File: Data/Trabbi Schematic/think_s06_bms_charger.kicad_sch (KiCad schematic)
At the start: 13 parts, among them J1 230V AC Mains Connection, K1 230V Relay, K2 Charge Cooling Relay R4, M1 Radiator Fan A (E11A), M2 Radiator Fan B (E11B), M3 Coolant Pump (E16), SW1 Charge Current Switch, U1 Battery Monitoring System (E0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, U2 Charger (E03)

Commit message: Fix wire-to-pin connections: use exact calculated pin positions
Refactored gen_think_complete.py to compute exact pin schematic
coordinates instead of using approximate manual offsets. Added p()
method to Sheet class that transforms symbol-local pin positions to
schematic coordinates. All 232 wire calls across 13 sub-sheet
generators now use p() for pin endpoints, fixing misaligned
connections (previously off by 0.54-10+ units).

Co-Authored-By: Claude Opus 4.6 <noreply@anthropic.com>
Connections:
- net +114V_CHARGER: now also U2.4 (+114V_DC)
- net +12V_F10_WPUMP_CHG: now also M3.1 (M+)
- net +12V_F28_DRIVE: now also U1.1 (BAT_12V)
- net +12V_F6_RADFAN: now also M1.1 (M+), M2.1 (M+)
- net -114V_CHARGER: now also U2.5 (-114V_DC)
- net BATT_COOLING: now also K2.1 (86_COIL+), U1.13 (BATT_COOLING)
- net BMS_CMD: now also U1.7 (BMS_CMD)
- net CHG_START: now also U2.6 (CHG_START)
- net CHG_START_IN: now also U1.4 (CHG_START_IN)
- net CHG_START_OUT: now also U1.6 (CHG_START_OUT)
- net CHG_STATUS_OK: now also U1.5 (CHG_STATUS_OK), U2.7 (CHG_STATUS_OK)
- net CURR_SENSE: now also U1.12 (CURR_SENSE)
- net CURR_S_12V: now also U1.10 (CURR_S_12V)
- net CURR_S_GND: now also U1.11 (CURR_S_GND)
- net DC_LO_PWR: now also U1.3 (DC_LO_PWR)
- net GND: now also M1.2 (M-), M2.2 (M-), M3.2 (M-), U1.2 (BAT_GND)
- net GND_AC: now also U2.3 (GND_AC)
- net K_LINE: now also U1.8 (K_LINE), U2.8 (K_LINE)
- net L1_AC: now also U2.1 (L1_AC)
- net L2_AC: now also U2.2 (L2_AC)
- net L_LINE: now also U1.9 (L_LINE), U2.9 (L_LINE)
- net TEMP1: now also RT1.1 (T+), U1.14 (TEMP1)
- net TEMP2: now also RT2.1 (T+), U1.15 (TEMP2)
- net TEMP3: now also RT3.1 (T+), U1.16 (TEMP3)
- net TEMP4: now also RT4.1 (T+), U1.17 (TEMP4)
- net at J1.1 (L1): now also K1.3 (30_COM)

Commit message: Enforce orthogonal routing and 1.27mm grid alignment
- Add _g() grid snap function to Sheet class (rounds all coordinates to nearest 1.27mm)
- Add wire_l() method for L-shaped orthogonal routing (horizontal+vertical segments)
- Apply grid snapping in p(), place(), wire(), label(), glabel(), junction(), no_connect(), defsym()
- Replace all 19 diagonal wire calls with wire_l() across S02, S06, S07, S08, S10, S12, S13
- All wire segments now strictly horizontal or vertical, no diagonals
- All coordinates verified on 1.27mm (50mil) KiCad standard grid

Co-Authored-By: Claude Opus 4.6 <noreply@anthropic.com>
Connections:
- net TEMP2 is gone; now on net TEMP1: RT2.1 (T+), U1.15 (TEMP2)
- net TEMP3 is gone; now on net TEMP1: RT3.1 (T+), U1.16 (TEMP3)
- net TEMP4 is gone; now on net TEMP1: RT4.1 (T+), U1.17 (TEMP4)
- net 230V_L1: now also J1.1 (L1), K1.3 (30_COM)

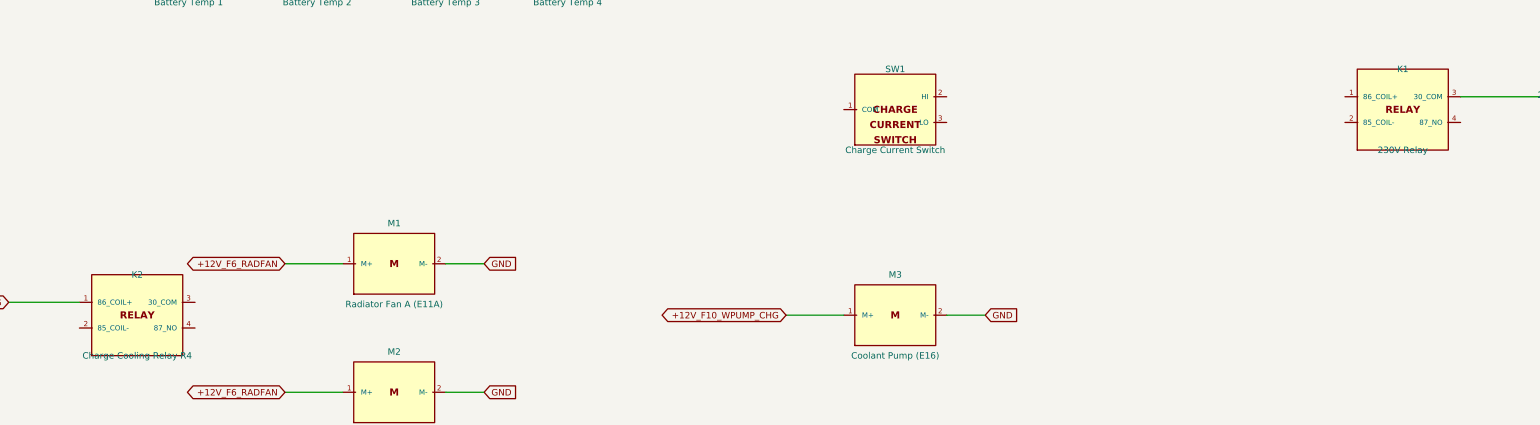
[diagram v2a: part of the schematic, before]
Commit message: Add relay coil/switch graphics, fix label positioning
- Draw coil (inductor arcs) and switch contacts (circles + arm)
  inside RELAY_SPST and RELAY_SPDT symbol bodies
- Add body_gfx parameter to defsym() for custom symbol graphics
- Helper functions: _gfx_polyline, _gfx_arc, _gfx_circle, _relay_gfx
- Fix label offsets: increase from 3-5mm to 10-12mm to avoid
  overlapping pin names (S01 ignition, S02 HV, S05 DCDC, S07 lights)
- Fix S09 turn signal rear labels: add wire stubs (were at 0 offset)
- All 14 schematics regenerated, parentheses balanced, grid OK

Co-Authored-By: Claude Opus 4.6 <noreply@anthropic.com>
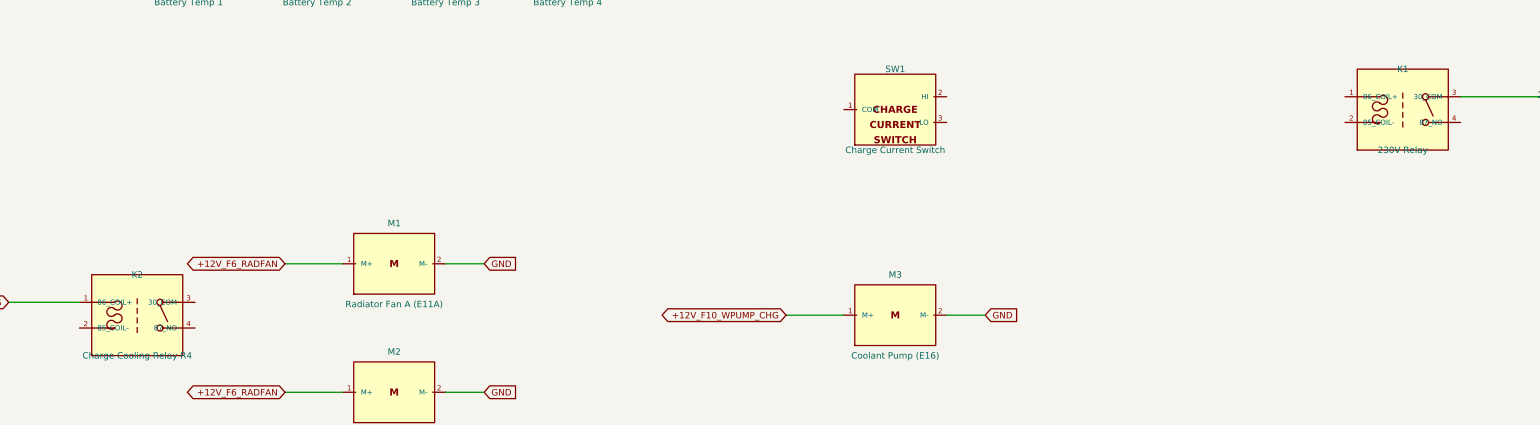
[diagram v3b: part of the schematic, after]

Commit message: Fix label/text positioning: Ref/Value outside body, hide pin numbers
- Reference placed above body edge, Value below (dynamic based on
  symbol height) — no longer overlapping body text
- Pin numbers hidden (clutter, not useful in schematic view)
- Pin name font reduced from 1.016mm to 0.762mm (less overlap)
- Pin length increased from 2.54mm to 3.81mm (more room for pin names
  between body edge and endpoint)
- Store symbol dimensions in _sym_dims for dynamic property placement

Co-Authored-By: Claude Opus 4.6 <noreply@anthropic.com>
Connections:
- net TEMP1: now also RT2.2 (T-)

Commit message: Add cross-sheet reference annotations to global labels
- Track all global label positions per sheet during build
- After building all sheets, annotate each global label with
  "→S01,S03,..." text showing which other sheets share the net
- 60 cross-sheet nets identified and annotated
- Two-pass build: 1) build all sheets 2) add cross-refs + save
- Text placed near label in 0.8mm font, offset to avoid overlap

Co-Authored-By: Claude Opus 4.6 <noreply@anthropic.com>
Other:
- note added: "→S01"
- note added: "→S01,S02,S03,S04,S05,S07,S08,S09,S10,S11,S12,S13"
- note added: "→S01,S02,S13"
- note added: "→S01,S11"
- note added: "→S02,S03,S11"
- note added: "→S02,S03,S11,S13"
- note added: "→S02,S03,S13"
- note added: "→S02,S13"
- note added: "→S03"
- note added: "→S05"
- note added: "→S11"
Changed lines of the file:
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@@
     (effects (font (size 1.000 1.000)))
+  )
+  (text "→S01,S02,S13" (at 56.690 86.320 0)
+    (effects (font (size 0.800 0.800)))
+  )
+  (text "→S01,S02,S03,S04,S05,S07,S08,S09,S10,S11,S12,S13" (at 56.690 97.750 0)
+    (effects (font (size 0.800 0.800)))
+  )
+  (text "→S01,S02,S03,S04,S05,S07,S08,S09,S10,S11,S12,S13" (at 122.380 232.370 0)
+    (effects (font (size 0.800 0.800)))
+  )
+  (text "→S01,S02,S03,S04,S05,S07,S08,S09,S10,S11,S12,S13" (at 122.380 257.770 0)
+    (effects (font (size 0.800 0.800)))
+  )
+  (text "→S01,S02,S03,S04,S05,S07,S08,S09,S10,S11,S12,S13" (at 221.440 242.530 0)
+    (effects (font (size 0.800 0.800)))
+  )
+  (text "→S05" (at 56.690 107.910 0)
+    (effects (font (size 0.800 0.800)))
+  )
+  (text "→S03" (at 143.970 85.050 0)
+    (effects (font (size 0.800 0.800)))
+  )
+  (text "→S03" (at 297.640 61.500 0)
+    (effects (font (size 0.800 0.800)))
+  )
+  (text "→S02,S03,S13" (at 143.970 102.830 0)
+    (effects (font (size 0.800 0.800)))
+  )
+  (text "→S02,S03,S11,S13" (at 143.970 111.720 0)
+    (effects (font (size 0.800 0.800)))
+  )
+  (text "→S02,S03,S11,S13" (at 307.800 139.160 0)
+    (effects (font (size 0.800 0.800)))
+  )
+  (text "→S02,S03,S11" (at 143.970 120.610 0)
+    (effects (font (size 0.800 0.800)))
+  )
+  (text "→S02,S03,S11" (at 297.640 139.160 0)
+    (effects (font (size 0.800 0.800)))
+  )
+  (text "→S11" (at 91.900 55.150 0)
+    (effects (font (size 0.800 0.800)))
+  )
+  (text "→S11" (at 19.860 239.990 0)
+    (effects (font (size 0.800 0.800)))
+  )
+  (text "→S05" (at 337.010 96.480 0)
+    (effects (font (size 0.800 0.800)))
+  )
+  (text "→S05" (at 337.010 109.180 0)
+    (effects (font (size 0.800 0.800)))
+  )
+  (text "→S02,S13" (at 307.800 61.500 0)
+    (effects (font (size 0.800 0.800)))
+  )
+  (text "→S01" (at 74.470 232.370 0)
+    (effects (font (size 0.800 0.800)))
+  )
+  (text "→S01" (at 74.470 257.770 0)
+    (effects (font (size 0.800 0.800)))
+  )
+  (text "→S01,S11" (at 173.530 242.530 0)
+    (effects (font (size 0.800 0.800)))
   )
   (symbol_instances)

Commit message: Fix label text justification for KiCad 9
Add (justify left) to all label and global_label effects.
KiCad 9 requires explicit text justification — without it,
label text is mispositioned relative to the label shape.

Co-Authored-By: Claude Opus 4.6 <noreply@anthropic.com>
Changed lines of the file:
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@@
   )
   (global_label "+12V_F28_DRIVE" (shape bidirectional) (at 59.690 83.820 180)
-    (effects (font (size 1.27 1.27)))
+    (effects (font (size 1.27 1.27)) (justify left))
     (property "Intersheetrefs" "${INTERSHEET_REFS}" (at 59.690 83.820 0)
       (effects (font (size 1.27 1.27)) hide)
@@
   )
   (global_label "GND" (shape input) (at 59.690 95.250 180)
-    (effects (font (size 1.27 1.27)))
+    (effects (font (size 1.27 1.27)) (justify left))
     (property "Intersheetrefs" "${INTERSHEET_REFS}" (at 59.690 95.250 0)
       (effects (font (size 1.27 1.27)) hide)
@@
   )
   (global_label "DC_LO_PWR" (shape bidirectional) (at 59.690 105.410 180)
-    (effects (font (size 1.27 1.27)))
+    (effects (font (size 1.27 1.27)) (justify left))
     (property "Intersheetrefs" "${INTERSHEET_REFS}" (at 59.690 105.410 0)
       (effects (font (size 1.27 1.27)) hide)
@@
   )
   (global_label "CHG_START_IN" (shape bidirectional) (at 59.690 116.840 180)
-    (effects (font (size 1.27 1.27)))
+    (effects (font (size 1.27 1.27)) (justify left))
     (property "Intersheetrefs" "${INTERSHEET_REFS}" (at 59.690 116.840 0)
       (effects (font (size 1.27 1.27)) hide)
@@
   )
   (global_label "CHG_STATUS_OK" (shape bidirectional) (at 140.970 82.550 0)
-    (effects (font (size 1.27 1.27)))
+    (effects (font (size 1.27 1.27)) (justify left))
     (property "Intersheetrefs" "${INTERSHEET_REFS}" (at 140.970 82.550 0)
       (effects (font (size 1.27 1.27)) hide)
@@
   )
   (global_label "CHG_START_OUT" (shape bidirectional) (at 140.970 91.440 0)
-    (effects (font (size 1.27 1.27)))
+    (effects (font (size 1.27 1.27)) (justify left))
     (property "Intersheetrefs" "${INTERSHEET_REFS}" (at 140.970 91.440 0)
       (effects (font (size 1.27 1.27)) hide)
@@
   )
   (global_label "BMS_CMD" (shape bidirectional) (at 140.970 100.330 0)
-    (effects (font (size 1.27 1.27)))
+    (effects (font (size 1.27 1.27)) (justify left))
     (property "Intersheetrefs" "${INTERSHEET_REFS}" (at 140.970 100.330 0)
       (effects (font (size 1.27 1.27)) hide)
@@
   )
   (global_label "K_LINE" (shape bidirectional) (at 140.970 109.220 0)
-    (effects (font (size 1.27 1.27)))
+    (effects (font (size 1.27 1.27)) (justify left))
     (property "Intersheetrefs" "${INTERSHEET_REFS}" (at 140.970 109.220 0)
       (effects (font (size 1.27 1.27)) hide)
@@
   )
   (global_label "L_LINE" (shape bidirectional) (at 140.970 118.110 0)
-    (effects (font (size 1.27 1.27)))
+    (effects (font (size 1.27 1.27)) (justify left))
     (property "Intersheetrefs" "${INTERSHEET_REFS}" (at 140.970 118.110 0)
       (effects (font (size 1.27 1.27)) hide)
@@
   )
   (global_label "CURR_S_12V" (shape bidirectional) (at 111.760 57.150 90)
-    (effects (font (size 1.27 1.27)))
+    (effects (font (size 1.27 1.27)) (justify left))
     (property "Intersheetrefs" "${INTERSHEET_REFS}" (at 111.760 57.150 0)
       (effects (font (size 1.27 1.27)) hide)
@@
   )
   (global_label "CURR_S_GND" (shape bidirectional) (at 104.140 57.150 90)
-    (effects (font (size 1.27 1.27)))
+    (effects (font (size 1.27 1.27)) (justify left))
     (property "Intersheetrefs" "${INTERSHEET_REFS}" (at 104.140 57.150 0)
       (effects (font (size 1.27 1.27)) hide)
@@
   )
   (global_label "CURR_SENSE" (shape bidirectional) (at 96.520 57.150 90)
-    (effects (font (size 1.27 1.27)))
+    (effects (font (size 1.27 1.27)) (justify left))
     (property "Intersheetrefs" "${INTERSHEET_REFS}" (at 96.520 57.150 0)
       (effects (font (size 1.27 1.27)) hide)
@@
   )
   (global_label "BATT_COOLING" (shape bidirectional) (at 88.900 57.150 90)
-    (effects (font (size 1.27 1.27)))
+    (effects (font (size 1.27 1.27)) (justify left))
     (property "Intersheetrefs" "${INTERSHEET_REFS}" (at 88.900 57.150 0)
       (effects (font (size 1.27 1.27)) hide)
@@
   )
   (label "TEMP1" (at 111.760 142.240 0)
-    (effects (font (size 1.27 1.27)))
+    (effects (font (size 1.27 1.27)) (justify left))
   )
   (wire (pts (xy 111.760 142.240) (xy 111.760 170.180))
@@
   )
   (label "TEMP2" (at 104.140 142.240 0)
-    (effects (font (size 1.27 1.27)))
+    (effects (font (size 1.27 1.27)) (justify left))
   )
   (wire (pts (xy 104.140 142.240) (xy 104.140 170.180))
@@
   )
   (label "TEMP3" (at 96.520 142.240 0)
-    (effects (font (size 1.27 1.27)))
+    (effects (font (size 1.27 1.27)) (justify left))
   )
   (wire (pts (xy 96.520 142.240) (xy 96.520 170.180))
@@
   )
   (label "TEMP4" (at 88.900 142.240 0)
-    (effects (font (size 1.27 1.27)))
+    (effects (font (size 1.27 1.27)) (justify left))
   )
   (wire (pts (xy 88.900 142.240) (xy 88.900 170.180))
@@
   )
   (label "L1_AC" (at 267.970 90.170 0)
-    (effects (font (size 1.27 1.27)))
+    (effects (font (size 1.27 1.27)) (justify left))
   )
   (wire (pts (xy 280.670 100.330) (xy 267.970 100.330))
@@
   )
   (label "L2_AC" (at 267.970 100.330 0)
-    (effects (font (size 1.27 1.27)))
+    (effects (font (size 1.27 1.27)) (justify left))
   )
   (wire (pts (xy 280.670 110.490) (xy 267.970 110.490))
@@
   )
   (label "GND_AC" (at 267.970 110.490 0)
-    (effects (font (size 1.27 1.27)))
+    (effects (font (size 1.27 1.27)) (justify left))
   )
   (wire (pts (xy 318.770 93.980) (xy 334.010 93.980))
@@
   )
   (global_label "+114V_CHARGER" (shape bidirectional) (at 334.010 93.980 0)
-    (effects (font (size 1.27 1.27)))
+    (effects (font (size 1.27 1.27)) (justify left))
     (property "Intersheetrefs" "${INTERSHEET_REFS}" (at 334.010 93.980 0)
       (effects (font (size 1.27 1.27)) hide)
@@
   )
   (global_label "-114V_CHARGER" (shape bidirectional) (at 334.010 106.680 0)
-    (effects (font (size 1.27 1.27)))
+    (effects (font (size 1.27 1.27)) (justify left))
     (property "Intersheetrefs" "${INTERSHEET_REFS}" (at 334.010 106.680 0)
       (effects (font (size 1.27 1.27)) hide)
@@
   )
   (global_label "CHG_START" (shape bidirectional) (at 304.800 63.500 90)
-    (effects (font (size 1.27 1.27)))
+    (effects (font (size 1.27 1.27)) (justify left))
     (property "Intersheetrefs" "${INTERSHEET_REFS}" (at 304.800 63.500 0)
       (effects (font (size 1.27 1.27)) hide)
@@
   )
   (global_label "CHG_STATUS_OK" (shape bidirectional) (at 294.640 63.500 90)
-    (effects (font (size 1.27 1.27)))
+    (effects (font (size 1.27 1.27)) (justify left))
     (property "Intersheetrefs" "${INTERSHEET_REFS}" (at 294.640 63.500 0)
       (effects (font (size 1.27 1.27)) hide)
@@
   )
   (global_label "K_LINE" (shape bidirectional) (at 304.800 137.160 270)
-    (effects (font (size 1.27 1.27)))
+    (effects (font (size 1.27 1.27)) (justify left))
     (property "Intersheetrefs" "${INTERSHEET_REFS}" (at 304.800 137.160 0)
       (effects (font (size 1.27 1.27)) hide)
@@
   )
   (global_label "L_LINE" (shape bidirectional) (at 294.640 137.160 270)
-    (effects (font (size 1.27 1.27)))
+    (effects (font (size 1.27 1.27)) (justify left))
     (property "Intersheetrefs" "${INTERSHEET_REFS}" (at 294.640 137.160 0)
       (effects (font (size 1.27 1.27)) hide)
@@
   )
   (label "230V_L1" (at 327.660 196.850 0)
-    (effects (font (size 1.27 1.27)))
+    (effects (font (size 1.27 1.27)) (justify left))
   )
   (wire (pts (xy 36.830 237.490) (xy 22.860 237.490))
@@
   )
   (global_label "BATT_COOLING" (shape bidirectional) (at 22.860 237.490 180)
-    (effects (font (size 1.27 1.27)))
+    (effects (font (size 1.27 1.27)) (justify left))
     (property "Intersheetrefs" "${INTERSHEET_REFS}" (at 22.860 237.490 0)
       (effects (font (size 1.27 1.27)) hide)
@@
   )
   (global_label "+12V_F6_RADFAN" (shape bidirectional) (at 77.470 229.870 180)
-    (effects (font (size 1.27 1.27)))
+    (effects (font (size 1.27 1.27)) (justify left))
     (property "Intersheetrefs" "${INTERSHEET_REFS}" (at 77.470 229.870 0)
       (effects (font (size 1.27 1.27)) hide)
@@
   )
   (global_label "GND" (shape input) (at 119.380 229.870 0)
-    (effects (font (size 1.27 1.27)))
+    (effects (font (size 1.27 1.27)) (justify left))
     (property "Intersheetrefs" "${INTERSHEET_REFS}" (at 119.380 229.870 0)
       (effects (font (size 1.27 1.27)) hide)
@@
   )
   (global_label "+12V_F6_RADFAN" (shape bidirectional) (at 77.470 255.270 180)
-    (effects (font (size 1.27 1.27)))
+    (effects (font (size 1.27 1.27)) (justify left))
     (property "Intersheetrefs" "${INTERSHEET_REFS}" (at 77.470 255.270 0)
       (effects (font (size 1.27 1.27)) hide)
@@
   )
   (global_label "GND" (shape input) (at 119.380 255.270 0)
-    (effects (font (size 1.27 1.27)))
+    (effects (font (size 1.27 1.27)) (justify left))
     (property "Intersheetrefs" "${INTERSHEET_REFS}" (at 119.380 255.270 0)
       (effects (font (size 1.27 1.27)) hide)
@@
   )
   (global_label "+12V_F10_WPUMP_CHG" (shape bidirectional) (at 176.530 240.030 180)
-    (effects (font (size 1.27 1.27)))
+    (effects (font (size 1.27 1.27)) (justify left))
     (property "Intersheetrefs" "${INTERSHEET_REFS}" (at 176.530 240.030 0)
       (effects (font (size 1.27 1.27)) hide)
@@
   )
   (global_label "GND" (shape input) (at 218.440 240.030 0)
-    (effects (font (size 1.27 1.27)))
+    (effects (font (size 1.27 1.27)) (justify left))
     (property "Intersheetrefs" "${INTERSHEET_REFS}" (at 218.440 240.030 0)
       (effects (font (size 1.27 1.27)) hide)
